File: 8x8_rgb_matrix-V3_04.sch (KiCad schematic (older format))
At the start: 48 parts, among them IC1 ATMega328, IC2 74HC595 SMD, IC3 74HC595 SMD, IC4 74HC595 SMD, IC5 74HC595 SMD, P1 FTDI, P2 PORTC, P3 PORTD, P4 ICSP, P5 JMP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

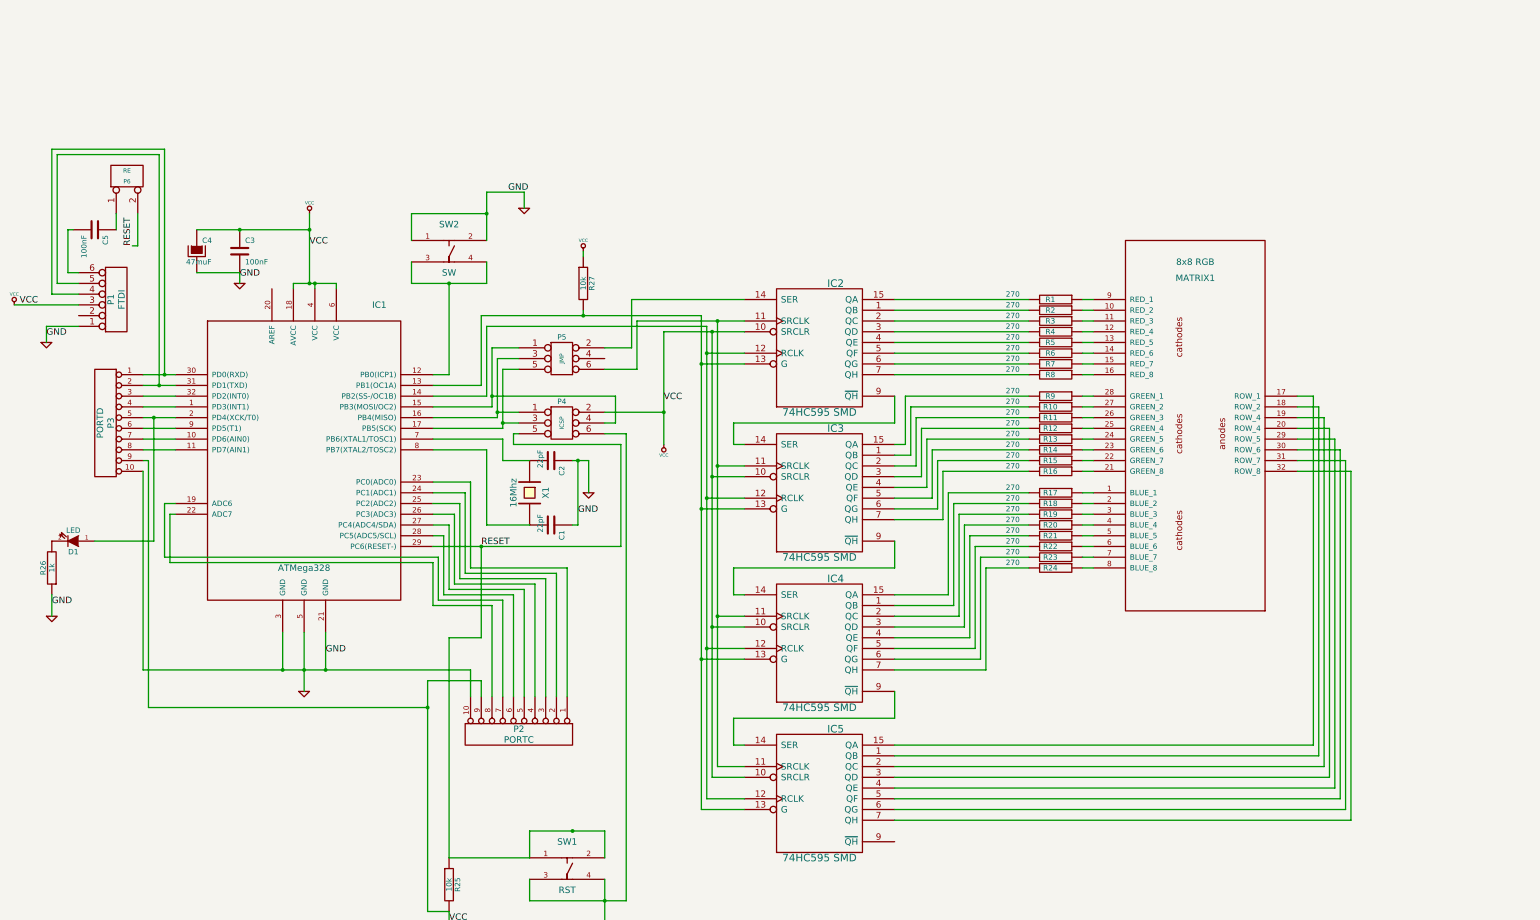
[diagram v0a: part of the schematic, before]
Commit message: Schematic fixed (pwr_flags, no-connects...) & LED-matrix (pins to passive).
All layout-related files unchanged.
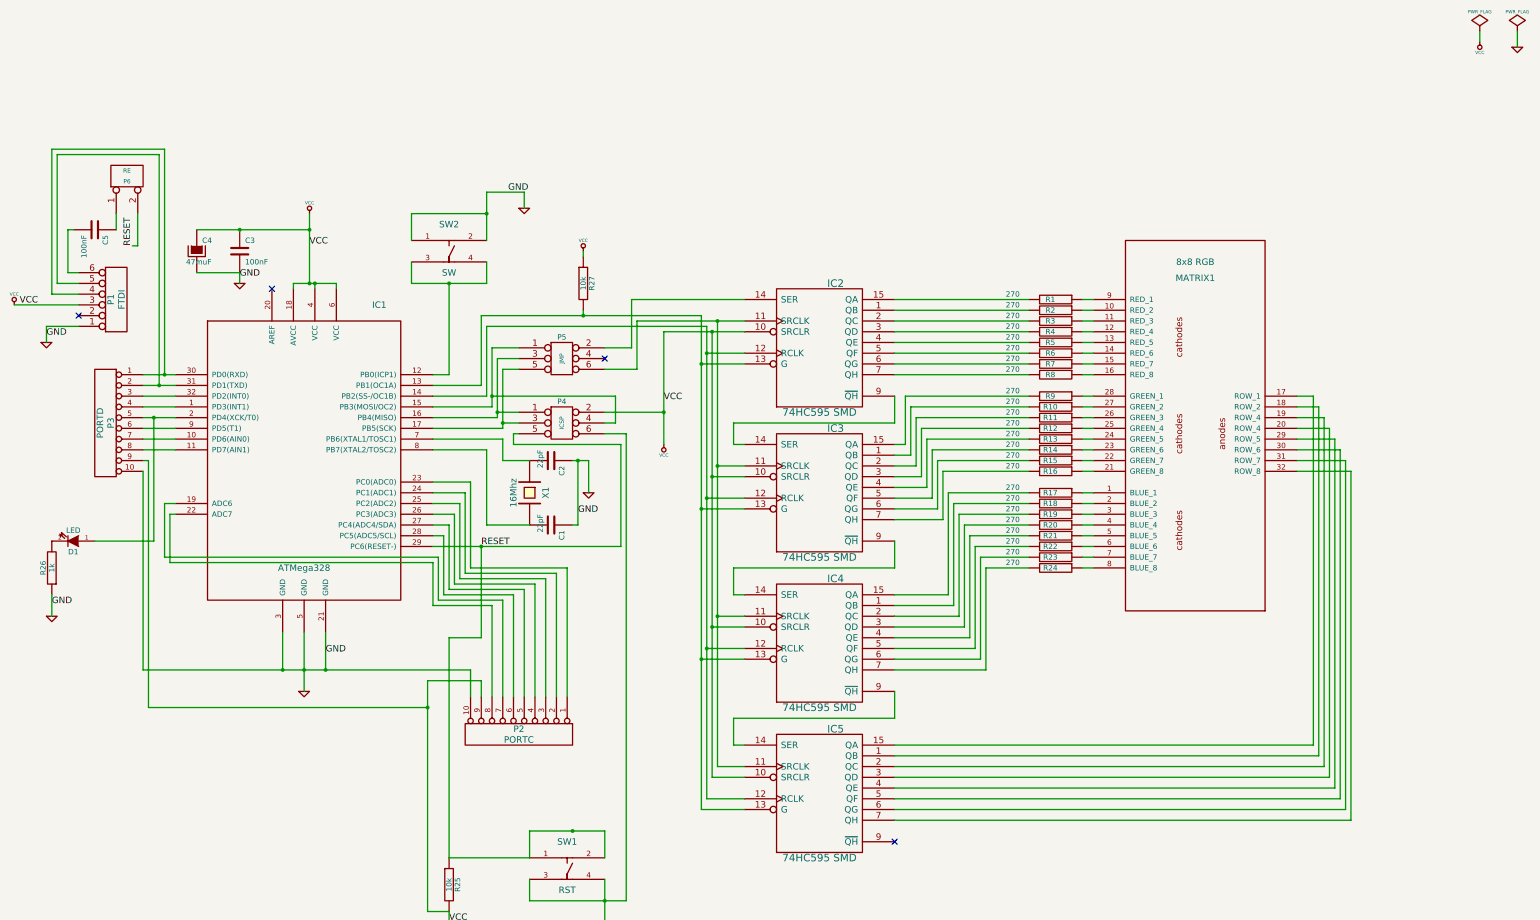
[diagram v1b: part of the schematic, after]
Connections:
- no-connect marks 0 -> 4
